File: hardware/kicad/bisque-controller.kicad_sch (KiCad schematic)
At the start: 49 parts, among them J1 USB-C, J2 5V_IN, J3 TC_K, J4 SSR, J5 DISPLAY, J6 NAV_SW, J7 AUX, Q1 AO3400A, Q2 AO3400A, SW1 RESET, SW2 BOOT, U1 ESP32-S3-WROOM-1-N16R8, U2 AMS1117-3.3, U3 MAX31855KASA+, U4 USBLC6-2SC6

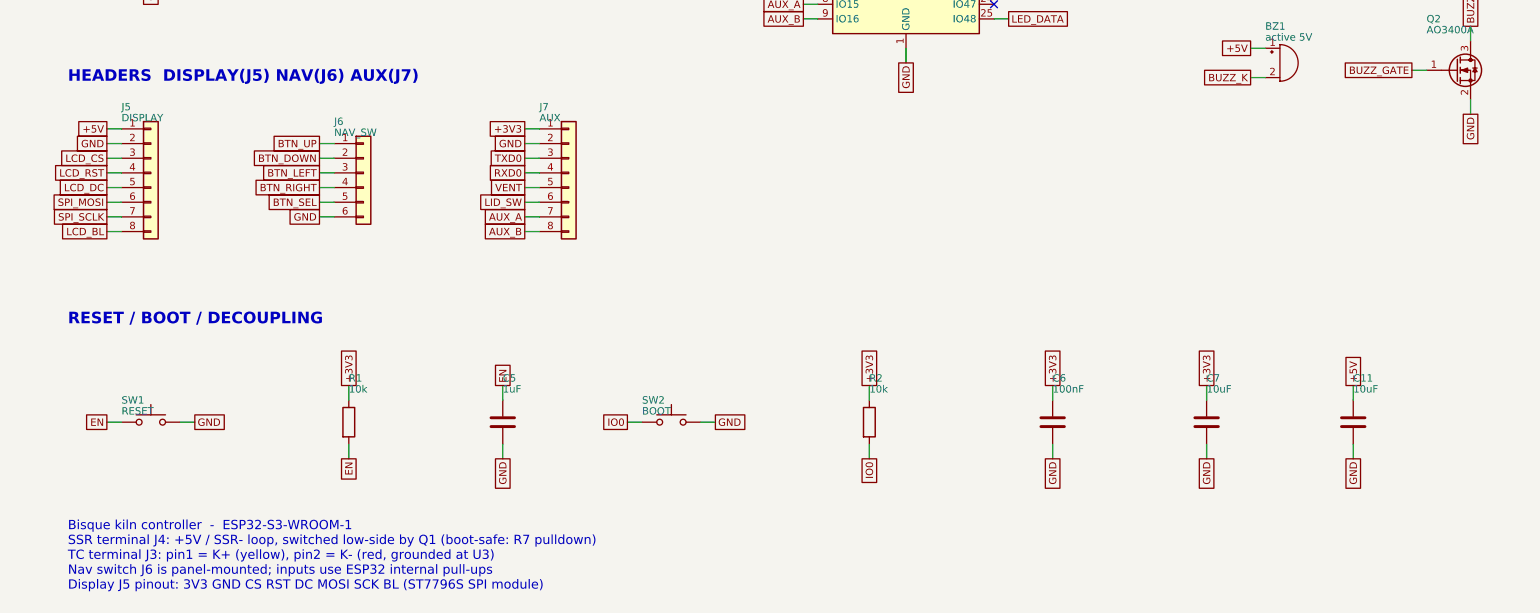
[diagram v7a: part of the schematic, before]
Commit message: hardware: filter the lid-switch input for the #83 interlock
Firmware issue #83 turns the previously-unused lid/door switch
(CONFIG_KILN_PIN_LID_SWITCH, IO21) into a firing interlock. The board
already routed the net -- LID_SW on ESP32-S3 pin 23 to aux header J7 pin
6 -- but as a bare GPIO on the ESP32's weak ~45k internal pull-up. It is
the one input whose cable leaves the enclosure and runs to a hot kiln
lid alongside the SSR output and mains wiring, and once #83 lands a
false "lid open" cuts a firing, so noise immunity now matters.

J7 pin 6 becomes a new net LID_IN and reaches U1.23 (LID_SW) through:

  R12  1k 0805   series -- fault/ESD current limit + RC series element
  R13  10k 0805  pull-up to +3V3, replacing the internal one
  C12  100nF     shunt to GND at the point of entry

Why this combination rather than the alternatives:

- A bare external pull-up alone leaves the pin's own clamp diodes as the
  only transient path. Adding C12 costs one Basic part and gives a real
  low-pass: ~1.8 kHz with the switch closed (C12 across R12||R13 ~ 0.9k),
  ~160 Hz open. The firmware samples at 500 ms and debounces in software,
  so the RC only has to kill fast EMI transients, not bounce.
- R12 is needed anyway to form that RC and to limit fault current if the
  lid cable ever shorts to something. Closed-switch level is
  3.3V x 1k/11k = 0.30V, well under the ESP32's 0.25 x VDD (0.83V) V_IL.
- R13 at 10k rather than the internal ~45k so an open switch holds the
  node high against leakage and capacitive pickup on a long cable. It
  also matches the 10k parts already on the board (R1, R2, R7, R8).
- No discrete TVS. The board's only one is the USBLC6 (U4), fitted for
  USB 2.0's low-capacitance requirement; the other externally exposed
  nets (TC_P at J3, the nav switch at J6) rely on an RC plus the pin's
  clamp diodes. A TVS here would be inconsistent with the rest of the
  board and would add a unique Extended part ($3 feeder fee) for one
  input.

Assembly cost is un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
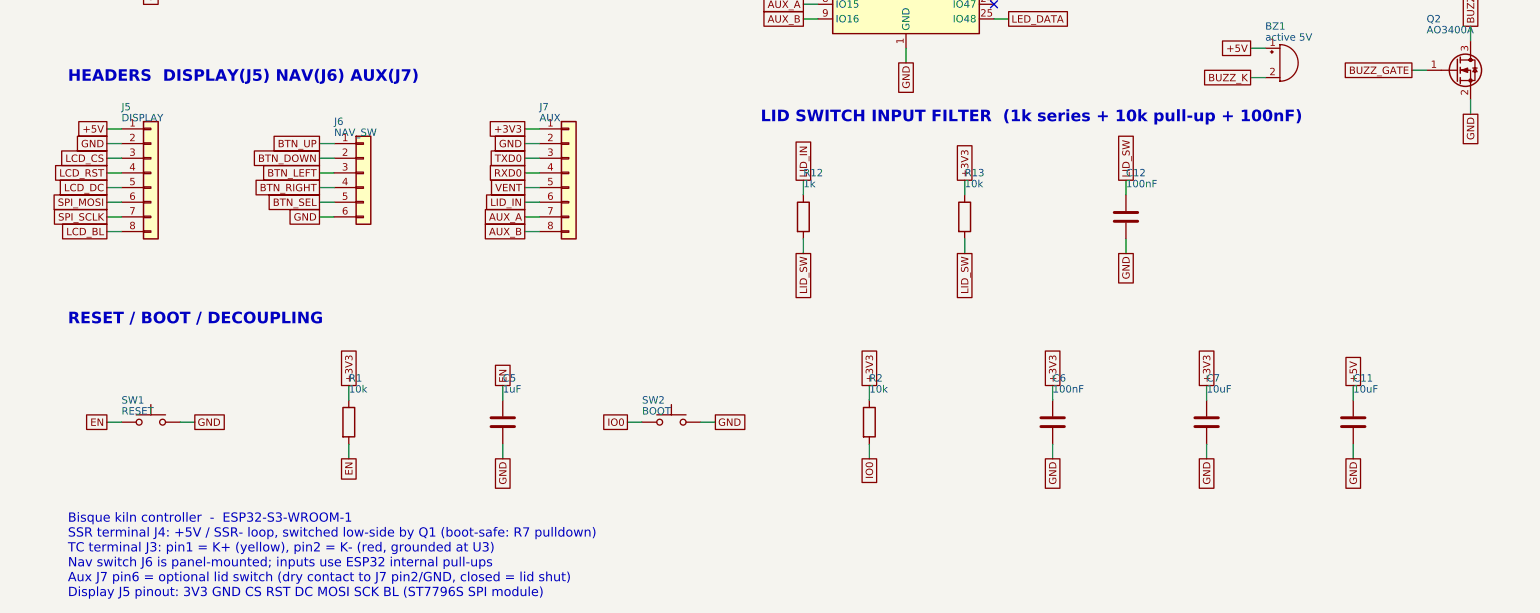
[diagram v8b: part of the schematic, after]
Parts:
- added C12: 100nF, Capacitor_SMD:C_0805_2012Metric, symbol Device:C
- added R12: 1k, Resistor_SMD:R_0805_2012Metric, symbol Device:R
- added R13: 10k, Resistor_SMD:R_0805_2012Metric, symbol Device:R
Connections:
- net +3V3: now also R13.1
- net GND: now also C12.2
- net LID_SW: now also C12.1, R12.2, R13.2; no longer J7.6 (Pin_6)
- new net LID_IN: J7.6 (Pin_6), R12.1
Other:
- note added: "Bisque kiln controller - ESP32-S3-WROOM-1 SSR terminal J4: +5V / SSR- loop, switched low-side by Q1 (boot-safe: R7 pulldown) TC terminal J3: pin1 = K+ (yellow), pin2 = K- (red, grounded at U3) Nav switch J6 is panel-mounted; inputs use ESP32 internal pull-ups Aux J7 pin6 = optional lid switch (dry contact to J7 pin2/GND, closed = lid shut) Display J5 pinout: 3V3 GND CS RST DC MOSI SCK BL (ST7796S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"
- note added: "LID SWITCH INPUT FILTER (1k series + 10k pull-up + 100nF)"
- note removed: "Bisque kiln controller - ESP32-S3-WROOM-1 SSR terminal J4: +5V / SSR- loop, switched low-side by Q1 (boot-safe: R7 pulldown) TC terminal J3: pin1 = K+ (yellow), pin2 = K- (red, grounded at U3) Nav switch J6 is panel-mounted; inputs use ESP32 internal pull-ups Display J5 pinout: 3V3 GND CS RST DC MOSI SCK BL (ST7796S SPI module)"
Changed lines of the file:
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@@
+		)
+	)
+	(symbol (lib_id "Device:R") (at 152.4 222.25 0) (unit 1)
+		(in_bom yes) (on_board yes) (dnp no)
+		(property "Reference" "R12" (at 152.4 214.63 0)
+			(effects (font (size 1.27 1.27)) (justify left))
+		)
+		(property "Value" "1k" (at 152.4 216.53 0)
+			(effects (font (size 1.27 1.27)) (justify left))
+		)
+		(property "Footprint" "Resistor_SMD:R_0805_2012Metric" (at 152.4 222.25 0)
+			(effects (font (size 1.27 1.27)) hide)
+		)
+		(property "Datasheet" "" (at 152.4 222.25 0)
+			(effects (font (size 1.27 1.27)) hide)
+		)
+		(property "Description" "Resistor" (at 152.4 222.25 0)
+			(effects (font (size 1.27 1.27)) hide)
+		)
+		(pin "1")
+		(pin "2")
+		(instances (project "bisque-controller" (path "/f24e0cd2-71c5-510c-9d15-562ab64c4388" (reference "R12") (unit 1))))
+	)
+	(wire (pts (xy 152.4 218.44) (xy 152.4 215.9))
+		(stroke (width 0) (type default))
+	)
+	(global_label "LID_IN" (shape passive) (at 152.4 215.9 90)
+		(effects (font (size 1.27 1.27)) (justify left))
+		(property "Intersheetrefs" "${INTERSHEET_REFS}" (at 152.4 215.9 0)
+			(effects (font (size 1.27 1.27)) hide)
+		)
+	)
+	(wire (pts (xy 152.4 226.06) (xy 152.4 228.6))
+		(stroke (width 0) (type default))
+	)
+	(global_label "LID_SW" (shape passive) (at 152.4 228.6 270)
+		(effects (font (size 1.27 1.27)) (justify right))
+		(property "Intersheetrefs" "${INTERSHEET_REFS}" (at 152.4 228.6 0)
+			(effects (font (size 1.27 1.27)) hide)
+		)
+	)
+	(symbol (lib_id "Device:R") (at 180.34 222.25 0) (unit 1)
+		(in_bom yes) (on_board yes) (dnp no)
+		(property "Reference" "R13" (at 180.34 214.63 0)
+			(effects (font (size 1.27 1.27)) (justify left))
+		)
+		(property "Value" "10k" (at 180.34 216.53 0)
+			(effects (font (size 1.27 1.27)) (justify left))
+		)
+		(property "Footprint" "Resistor_SMD:R_0805_2012Metric" (at 180.34 222.25 0)
+			(effects (font (size 1.27 1.27)) hide)
+		)
+		(property "Datasheet" "" (at 180.34 222.25 0)
+			(effects (font (size 1.27 1.27)) hide)
+		)
+		(property "Description" "Resistor" (at 180.34 222.25 0)
+			(effects (font (size 1.27 1.27)) hide)
+		)
+		(pin "1")
+		(pin "2")
+		(instances (project "bisque-controller" (path "/f24e0cd2-71c5-510c-9d15-562ab64c4388" (reference "R13") (unit 1))))
+	)
+	(wire (pts (xy 180.34 218.44) (xy 180.34 215.9))
+		(stroke (width 0) (type default))
+	)
+	(global_label "+3V3" (shape passive) (at 180.34 215.9 90)
+		(effects (font (size 1.27 1.27)) (justify left))
+		(property "Intersheetrefs" "${INTERSHEET_REFS}" (at 180.34 215.9 0)
+			(effects (font (size 1.27 1.27)) hide)
+		)
+	)
+	(wire (pts (xy 180.34 226.06) (xy 180.34 228.6))
+		(stroke (width 0) (type default))
+	)
+	(global_label "LID_SW" (shape passive) (at 180.34 228.6 270)
+		(effects (font (size 1.27 1.27)) (justify right))
+		(property "Intersheetrefs" "${INTERSHEET_REFS}" (at 180.34 228.6 0)
+			(effects (font (size 1.27 1.27)) hide)
+		)
+	)
+	(symbol (lib_id "Device:C") (at 208.28 222.25 0) (unit 1)
+		(in_bom yes) (on_board yes) (dnp no)
+		(property "Reference" "C12" (at 208.28 214.63 0)
+			(effects (font (size 1.27 1.27)) (justify left))
+		)
+		(property "Value" "100nF" (at 208.28 216.53 0)
+			(effects (font (size 1.27 1.27)) (justify left))
+		)
+		(property "Footprint" "Capacitor_SMD:C_0805_2012Metric" (at 208.28 222.25 0)
+			(effects (font (size 1.27 1.27)) hide)
+		)
+		(property "Datasheet" "" (at 208.28 222.25 0)
+			(effects (font (size 1.27 1.27)) hide)
+		)
+		(property "Description" "Unpolarized capacitor" (at 208.28 222.25 0)
+			(effects (font (size 1.27 1.27)) hide)
+		)
+		(pin "1")
+		(pin "2")
+		(instances (project "bisque-controller" (path "/f24e0cd2-71c5-510c-9d15-562ab64c4388" (reference "C12") (unit 1))))
+	)
+	(wire (pts (xy 208.28 218.44) (xy 208.28 215.9))
+		(stroke (width 0) (type default))
+	)
+	(global_label "LID_SW" (shape passive) (at 208.28 215.9 90)
+		(effects (font (size 1.27 1.27)) (justify left))
+		(property "Intersheetrefs" "${INTERSHEET_REFS}" (at 208.28 215.9 0)
+			(effects (font (size 1.27 1.27)) hide)
+		)
+	)
+	(wire (pts (xy 208.28 226.06) (xy 208.28 228.6))
+		(stroke (width 0) (type default))
+	)
+	(global_label "GND" (shape passive) (at 208.28 228.6 270)
+		(effects (font (size 1.27 1.27)) (justify right))
+		(property "Intersheetrefs" "${INTERSHEET_REFS}" (at 208.28 228.6 0)
+			(effects (font (size 1.27 1.27)) hide)
 		)
 	)
@@
 		(stroke (width 0) (type default))
 	)
-	(global_label "LID_SW" (shape passive) (at 104.14 219.71 180)
+	(global_label "LID_IN" (shape passive) (at 104.14 219.71 180)
 		(effects (font (size 1.27 1.27)) (justify right))
 		(property "Intersheetrefs" "${INTERSHEET_REFS}" (at 104.14 219.71 0)
@@
 		(effects (font (size 2 2) bold) (justify left))
 	)
+	(text "LID SWITCH INPUT FILTER  (1k series + 10k pull-up + 100nF)" (at 145 205 0)
+		(effects (font (size 2 2) bold) (justify left))
+	)
 	(text "RESET / BOOT / DECOUPLING" (at 25 240 0)
 		(effects (font (size 2 2) bold) (justify left))
@@
 		(effects (font (size 2 2) bold) (justify left))
 	)
-	(text "Bisque kiln controller  -  ESP32-S3-WROOM-1\nSSR terminal J4: +5V / SSR- loop, switched low-side by Q1 (boot-safe: R7 pulldown)\nTC terminal J3: pin1 = K+ (yellow), pin2 = K- (red, grounded at U3)\nNav switch J6 is panel-mounted; inputs use ESP32 internal pull-ups\nDisplay J5 pinout: 3V3 GND CS RST DC MOSI SCK BL (ST7796S SPI module)" (at 25 281 0)
+	(text "Bisque kiln controller  -  ESP32-S3-WROOM-1\nSSR terminal J4: +5V / SSR- loop, switched low-side by Q1 (boot-safe: R7 pulldown)\nTC terminal J3: pin1 = K+ (yellow), pin2 = K- (red, grounded at U3)\nNav switch J6 is panel-mounted; inputs use ESP32 internal pull-ups\nAux J7 pin6 = optional lid switch (dry contact to J7 pin2/GND, closed = lid shut)\nDisplay J5 pinout: 3V3 GND CS RST DC MOSI SCK BL (ST7796S SPI module)" (at 25 281 0)
 		(effects (font (size 1.6 1.6)) (justify left))
 	)
